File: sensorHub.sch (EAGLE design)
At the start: 11 parts

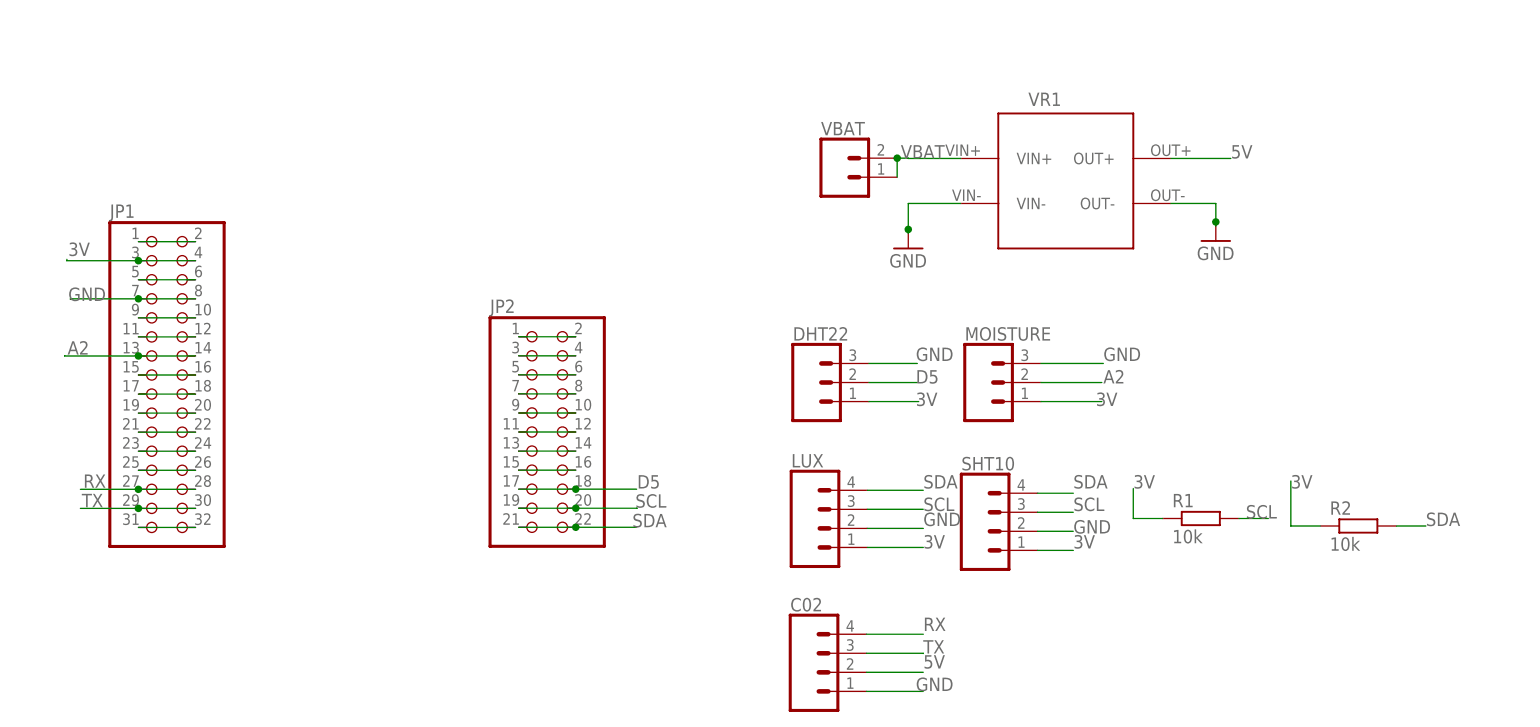
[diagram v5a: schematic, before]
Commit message: Connects the sht10 pins from SDA and SCL to pin 10 and pin 12 respectively
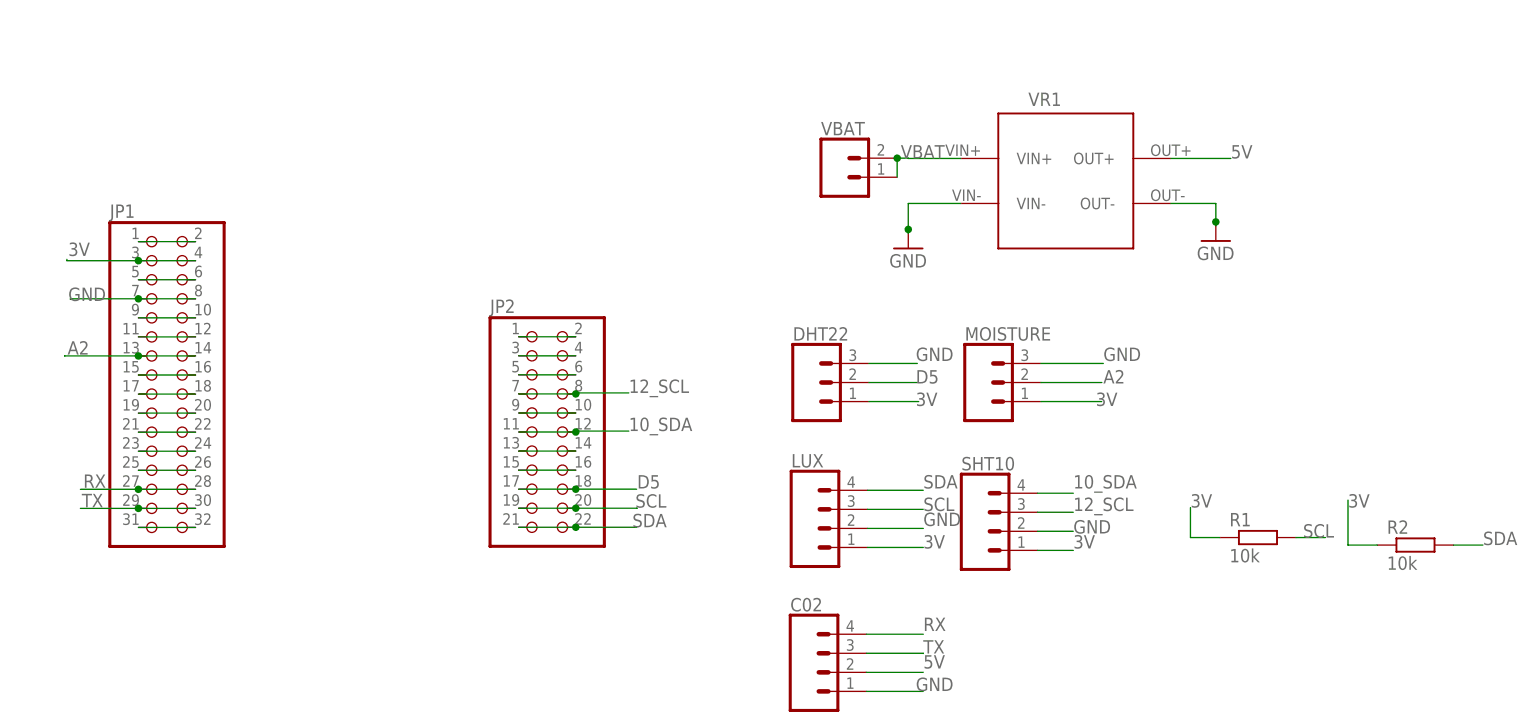
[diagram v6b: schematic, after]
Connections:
- removed net N$20: JP2.7, JP2.8
- removed net N$22: JP2.11, JP2.12
- new net 10_SDA: JP2.11, JP2.12, SHT10.4
- new net 12_SCL: JP2.7, JP2.8, SHT10.3
- net SCL: no longer SHT10.3
- net SDA: no longer SHT10.4
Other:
- moved on the sheet: R1, R2
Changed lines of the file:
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@@
 <attribute name="VALUE" x="132" y="95" size="1.778" layer="96"/>
 </instance>
-<instance part="R1" gate="G$1" x="155" y="62" smashed="yes">
-<attribute name="NAME" x="151.19" y="63.4986" size="1.778" layer="95"/>
-<attribute name="VALUE" x="151.19" y="58.698" size="1.778" layer="96"/>
-</instance>
-<instance part="R2" gate="G$1" x="176" y="61" smashed="yes">
-<attribute name="NAME" x="172.19" y="62.4986" size="1.778" layer="95"/>
-<attribute name="VALUE" x="172.19" y="57.698" size="1.778" layer="96"/>
+<instance part="R1" gate="G$1" x="162.62" y="59.46" smashed="yes">
+<attribute name="NAME" x="158.81" y="60.9586" size="1.778" layer="95"/>
+<attribute name="VALUE" x="158.81" y="56.158" size="1.778" layer="96"/>
+</instance>
+<instance part="R2" gate="G$1" x="183.62" y="58.46" smashed="yes">
+<attribute name="NAME" x="179.81" y="59.9586" size="1.778" layer="95"/>
+<attribute name="VALUE" x="179.81" y="55.158" size="1.778" layer="96"/>
 </instance>
 <instance part="DHT22" gate="J$1" x="103.14" y="80.13" smashed="yes">
@@
 <segment>
 <pinref part="R1" gate="G$1" pin="1"/>
-<wire x1="149.92" y1="62" x2="146" y2="62" width="0.1524" layer="91"/>
-<wire x1="146" y1="62" x2="146" y2="66" width="0.1524" layer="91"/>
-<label x="146" y="66" size="1.778" layer="95"/>
+<wire x1="157.54" y1="59.46" x2="153.62" y2="59.46" width="0.1524" layer="91"/>
+<wire x1="153.62" y1="59.46" x2="153.62" y2="63.46" width="0.1524" layer="91"/>
+<label x="153.62" y="63.46" size="1.778" layer="95"/>
 </segment>
 <segment>
 <pinref part="R2" gate="G$1" pin="1"/>
-<wire x1="170.92" y1="61" x2="167" y2="61" width="0.1524" layer="91"/>
-<wire x1="167" y1="61" x2="167" y2="67" width="0.1524" layer="91"/>
-<label x="167" y="66" size="1.778" layer="95"/>
+<wire x1="178.54" y1="58.46" x2="174.62" y2="58.46" width="0.1524" layer="91"/>
+<wire x1="174.62" y1="58.46" x2="174.62" y2="64.46" width="0.1524" layer="91"/>
+<label x="174.62" y="63.46" size="1.778" layer="95"/>
 </segment>
 </net>
@@
 </segment>
 </net>
-<net name="N$20" class="0">
-<segment>
-<pinref part="JP2" gate="A" pin="7"/>
-<pinref part="JP2" gate="A" pin="8"/>
-<wire x1="64.05" y1="78.61" x2="71.67" y2="78.61" width="0.1524" layer="91"/>
-</segment>
-</net>
 <net name="N$21" class="0">
 <segment>
@@
 <pinref part="JP2" gate="A" pin="10"/>
 <wire x1="64.05" y1="76.07" x2="71.67" y2="76.07" width="0.1524" layer="91"/>
-</segment>
-</net>
-<net name="N$22" class="0">
-<segment>
-<pinref part="JP2" gate="A" pin="11"/>
-<pinref part="JP2" gate="A" pin="12"/>
-<wire x1="64.05" y1="73.53" x2="71.67" y2="73.53" width="0.1524" layer="91"/>
 </segment>
 </net>
@@
 </segment>
 <segment>
-<pinref part="SHT10" gate="G$1" pin="3"/>
-<wire x1="133.23" y1="62.83" x2="138" y2="62.83" width="0.1524" layer="91"/>
-<label x="138" y="63" size="1.778" layer="95"/>
-</segment>
-<segment>
 <pinref part="R1" gate="G$1" pin="2"/>
-<wire x1="160.08" y1="62" x2="164" y2="62" width="0.1524" layer="91"/>
-<label x="161" y="62" size="1.778" layer="95"/>
+<wire x1="167.7" y1="59.46" x2="171.62" y2="59.46" width="0.1524" layer="91"/>
+<label x="168.62" y="59.46" size="1.778" layer="95"/>
 </segment>
 </net>
@@
 </segment>
 <segment>
-<pinref part="SHT10" gate="G$1" pin="4"/>
-<wire x1="133.23" y1="65.37" x2="138" y2="65.37" width="0.1524" layer="91"/>
-<label x="138" y="66" size="1.778" layer="95"/>
-</segment>
-<segment>
 <pinref part="R2" gate="G$1" pin="2"/>
-<wire x1="181.08" y1="61" x2="185" y2="61" width="0.1524" layer="91"/>
-<label x="185" y="61" size="1.778" layer="95"/>
+<wire x1="188.7" y1="58.46" x2="192.62" y2="58.46" width="0.1524" layer="91"/>
+<label x="192.62" y="58.46" size="1.778" layer="95"/>
 </segment>
 </net>
@@
 </segment>
 </net>
+<net name="10_SDA" class="0">
+<segment>
+<pinref part="SHT10" gate="G$1" pin="4"/>
+<wire x1="133.23" y1="65.37" x2="138" y2="65.37" width="0.1524" layer="91"/>
+<label x="138" y="66" size="1.778" layer="95"/>
+</segment>
+<segment>
+<pinref part="JP2" gate="A" pin="11"/>
+<pinref part="JP2" gate="A" pin="12"/>
+<wire x1="64.05" y1="73.53" x2="71.67" y2="73.53" width="0.1524" layer="91"/>
+<wire x1="71.67" y1="73.53" x2="71.67" y2="73.66" width="0.1524" layer="91"/>
+<wire x1="71.67" y1="73.66" x2="78.74" y2="73.66" width="0.1524" layer="91"/>
+<junction x="71.67" y="73.53"/>
+<label x="78.74" y="73.66" size="1.778" layer="95"/>
+</segment>
+</net>
+<net name="12_SCL" class="0">
+<segment>
+<pinref part="SHT10" gate="G$1" pin="3"/>
+<wire x1="133.23" y1="62.83" x2="138" y2="62.83" width="0.1524" layer="91"/>
+<label x="138" y="63" size="1.778" layer="95"/>
+</segment>
+<segment>
+<pinref part="JP2" gate="A" pin="7"/>
+<pinref part="JP2" gate="A" pin="8"/>
+<wire x1="64.05" y1="78.61" x2="71.67" y2="78.61" width="0.1524" layer="91"/>
+<wire x1="71.67" y1="78.61" x2="71.67" y2="78.74" width="0.1524" layer="91"/>
+<wire x1="71.67" y1="78.74" x2="78.74" y2="78.74" width="0.1524" layer="91"/>
+<junction x="71.67" y="78.61"/>
+<label x="78.74" y="78.74" size="1.778" layer="95"/>
+</segment>
+</net>

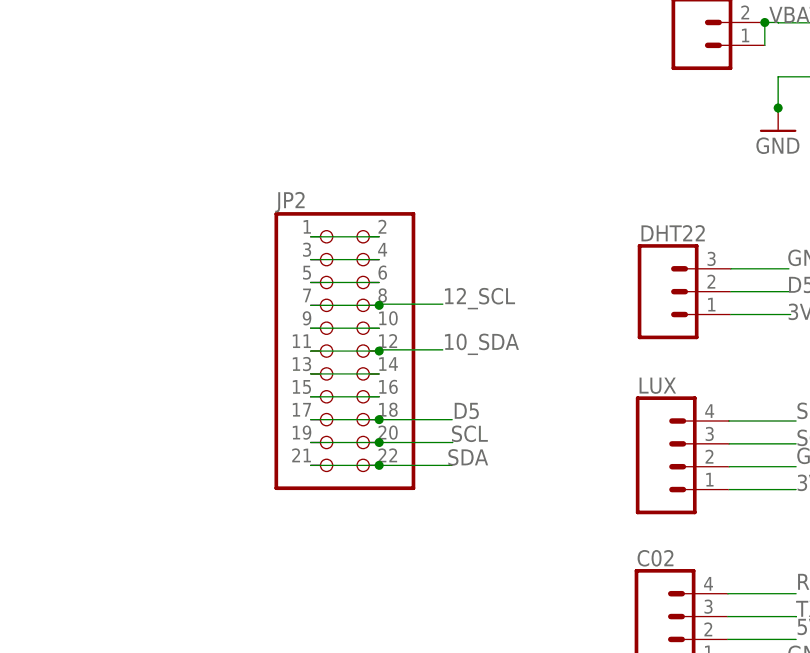
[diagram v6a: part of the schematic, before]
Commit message: Replaces the 22 double header with the 24 double header
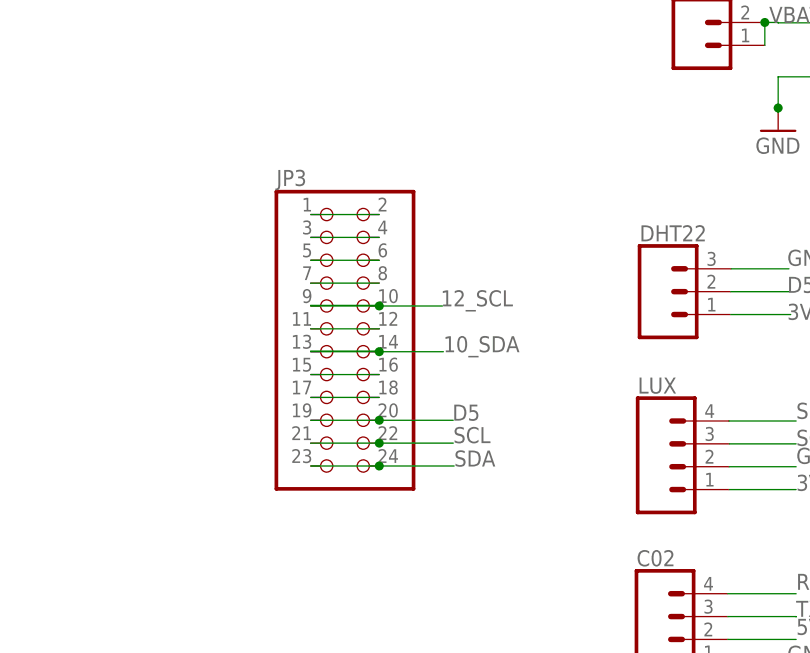
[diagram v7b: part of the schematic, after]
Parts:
- removed JP2: (no value), pinhead:PINHD-2X11
- added JP3: (no value), pinhead:PINHD-2X12
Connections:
- removed net N$19: JP2.5, JP2.6
- removed net N$21: JP2.10, JP2.9
- removed net N$23: JP2.13, JP2.14
- removed net N$24: JP2.15, JP2.16
- new net N$14: JP3.7, JP3.8
- new net N$15: JP3.11, JP3.12
- new net N$2: JP3.1, JP3.2
- new net N$4: JP3.3, JP3.4
- new net N$7: JP3.5, JP3.6
- net 10_SDA: now also JP3.13, JP3.14; no longer JP2.11, JP2.12
- net 12_SCL: now also JP3.10, JP3.9; no longer JP2.7, JP2.8
- net D5: now also JP3.19, JP3.20; no longer JP2.17, JP2.18
- net N$17: now also JP3.15, JP3.16; no longer JP2.1, JP2.2
- net N$18: now also JP3.17, JP3.18; no longer JP2.3, JP2.4
- net SCL: now also JP3.21, JP3.22; no longer JP2.19, JP2.20
- net SDA: now also JP3.23, JP3.24; no longer JP2.21, JP2.22
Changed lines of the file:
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@@
 <setting verticaltext="up"/>
 </settings>
-<grid distance="0.1" unitdist="inch" unit="inch" style="lines" multiple="1" display="no" altdistance="0.01" altunitdist="inch" altunit="inch"/>
+<grid distance="0.1" unitdist="mm" unit="mm" style="dots" multiple="1" display="yes" altdistance="1" altunitdist="mm" altunit="mm"/>
 <layers>
 <layer number="1" name="Top" color="4" fill="1" visible="no" active="no"/>
@@
 <parts>
 <part name="JP1" library="pinhead" library_urn="urn:adsk.eagle:library:325" deviceset="PINHD-2X16" device="" package3d_urn="urn:adsk.eagle:package:22431/2"/>
-<part name="JP2" library="pinhead" library_urn="urn:adsk.eagle:library:325" deviceset="PINHD-2X11" device="" package3d_urn="urn:adsk.eagle:package:22419/2"/>
 <part name="VR1" library="lm2577_module" deviceset="MT3608" device="THROUGH_HOLE"/>
 <part name="R1" library="resistor" library_urn="urn:adsk.eagle:library:348" deviceset="R-EU_" device="0207/10" package3d_urn="urn:adsk.eagle:package:25939/1" value="10k"/>
@@
 <part name="GND1" library="supply1" library_urn="urn:adsk.eagle:library:371" deviceset="GND" device=""/>
 <part name="GND2" library="supply1" library_urn="urn:adsk.eagle:library:371" deviceset="GND" device=""/>
+<part name="JP3" library="pinhead" library_urn="urn:adsk.eagle:library:325" deviceset="PINHD-2X12" device="" package3d_urn="urn:adsk.eagle:package:22420/2"/>
 </parts>
 <sheets>
@@
 <attribute name="VALUE" x="9.55" y="55.73" size="1.778" layer="96"/>
 </instance>
-<instance part="JP2" gate="A" x="66.59" y="73.53" smashed="yes">
-<attribute name="NAME" x="60.24" y="89.405" size="1.778" layer="95"/>
-<attribute name="VALUE" x="60.24" y="55.75" size="1.778" layer="96"/>
-</instance>
 <instance part="VR1" gate="G$1" x="137" y="107" smashed="yes">
 <attribute name="NAME" x="132" y="117" size="1.778" layer="95"/>
@@
 <instance part="GND2" gate="1" x="157" y="99" smashed="yes">
 <attribute name="VALUE" x="154.46" y="96.46" size="1.778" layer="96"/>
+</instance>
+<instance part="JP3" gate="A" x="66.6" y="76" smashed="yes">
+<attribute name="NAME" x="60.25" y="91.875" size="1.778" layer="95"/>
+<attribute name="VALUE" x="60.25" y="55.68" size="1.778" layer="96"/>
 </instance>
 </instances>
@@
 </segment>
 </net>
-<net name="N$17" class="0">
-<segment>
-<pinref part="JP2" gate="A" pin="1"/>
-<pinref part="JP2" gate="A" pin="2"/>
-<wire x1="64.05" y1="86.23" x2="71.67" y2="86.23" width="0.1524" layer="91"/>
-</segment>
-</net>
-<net name="N$18" class="0">
-<segment>
-<pinref part="JP2" gate="A" pin="3"/>
-<pinref part="JP2" gate="A" pin="4"/>
-<wire x1="64.05" y1="83.69" x2="71.67" y2="83.69" width="0.1524" layer="91"/>
-</segment>
-</net>
-<net name="N$19" class="0">
-<segment>
-<pinref part="JP2" gate="A" pin="5"/>
-<pinref part="JP2" gate="A" pin="6"/>
-<wire x1="64.05" y1="81.15" x2="71.67" y2="81.15" width="0.1524" layer="91"/>
-</segment>
-</net>
-<net name="N$21" class="0">
-<segment>
-<pinref part="JP2" gate="A" pin="9"/>
-<pinref part="JP2" gate="A" pin="10"/>
-<wire x1="64.05" y1="76.07" x2="71.67" y2="76.07" width="0.1524" layer="91"/>
-</segment>
-</net>
-<net name="N$23" class="0">
-<segment>
-<pinref part="JP2" gate="A" pin="13"/>
-<pinref part="JP2" gate="A" pin="14"/>
-<wire x1="64.05" y1="70.99" x2="71.67" y2="70.99" width="0.1524" layer="91"/>
-</segment>
-</net>
-<net name="N$24" class="0">
-<segment>
-<pinref part="JP2" gate="A" pin="15"/>
-<pinref part="JP2" gate="A" pin="16"/>
-<wire x1="64.05" y1="68.45" x2="71.67" y2="68.45" width="0.1524" layer="91"/>
-</segment>
-</net>
 <net name="D5" class="0">
-<segment>
-<pinref part="JP2" gate="A" pin="17"/>
-<pinref part="JP2" gate="A" pin="18"/>
-<wire x1="64.05" y1="65.91" x2="71.67" y2="65.91" width="0.1524" layer="91"/>
-<wire x1="71.67" y1="65.91" x2="79.79" y2="65.91" width="0.1524" layer="91"/>
-<junction x="71.67" y="65.91"/>
-<label x="79.85" y="66" size="1.778" layer="95"/>
-</segment>
 <segment>
 <pinref part="DHT22" gate="J$1" pin="2"/>
@@
 <label x="117" y="80" size="1.778" layer="95"/>
 </segment>
+<segment>
+<pinref part="JP3" gate="A" pin="19"/>
+<pinref part="JP3" gate="A" pin="20"/>
+<wire x1="64.06" y1="65.84" x2="71.68" y2="65.84" width="0.1524" layer="91"/>
+<wire x1="71.68" y1="65.84" x2="79.9" y2="65.84" width="0.1524" layer="91"/>
+<junction x="71.68" y="65.84"/>
+<label x="79.8" y="65.8" size="1.778" layer="95"/>
+</segment>
 </net>
 <net name="SCL" class="0">
-<segment>
-<pinref part="JP2" gate="A" pin="19"/>
-<pinref part="JP2" gate="A" pin="20"/>
-<wire x1="64.05" y1="63.37" x2="71.67" y2="63.37" width="0.1524" layer="91"/>
-<wire x1="71.67" y1="63.37" x2="79.83" y2="63.37" width="0.1524" layer="91"/>
-<wire x1="79.83" y1="63.37" x2="79.83" y2="63.39" width="0.1524" layer="91"/>
-<junction x="71.67" y="63.37"/>
-<label x="79.61" y="63.45" size="1.778" layer="95"/>
-</segment>
 <segment>
 <pinref part="LUX" gate="G$1" pin="3"/>
@@
 <label x="168.62" y="59.46" size="1.778" layer="95"/>
 </segment>
+<segment>
+<pinref part="JP3" gate="A" pin="21"/>
+<pinref part="JP3" gate="A" pin="22"/>
+<wire x1="64.06" y1="63.3" x2="71.68" y2="63.3" width="0.1524" layer="91"/>
+<wire x1="71.68" y1="63.3" x2="79.9" y2="63.3" width="0.1524" layer="91"/>
+<junction x="71.68" y="63.3"/>
+<label x="79.9" y="63.3" size="1.778" layer="95"/>
+</segment>
 </net>
 <net name="SDA" class="0">
-<segment>
-<pinref part="JP2" gate="A" pin="21"/>
-<pinref part="JP2" gate="A" pin="22"/>
-<wire x1="64.05" y1="60.83" x2="71.67" y2="60.83" width="0.1524" layer="91"/>
-<wire x1="71.67" y1="60.83" x2="79.79" y2="60.83" width="0.1524" layer="91"/>
-<junction x="71.67" y="60.83"/>
-<label x="79.21" y="60.83" size="1.778" layer="95"/>
-</segment>
 <segment>
 <pinref part="LUX" gate="G$1" pin="4"/>
@@
 <wire x1="188.7" y1="58.46" x2="192.62" y2="58.46" width="0.1524" layer="91"/>
 <label x="192.62" y="58.46" size="1.778" layer="95"/>
+</segment>
+<segment>
+<pinref part="JP3" gate="A" pin="23"/>
+<pinref part="JP3" gate="A" pin="24"/>
+<wire x1="64.06" y1="60.76" x2="71.68" y2="60.76" width="0.1524" layer="91"/>
+<wire x1="71.68" y1="60.76" x2="80" y2="60.76" width="0.1524" layer="91"/>
+<junction x="71.68" y="60.76"/>
+<label x="80" y="60.7" size="1.778" layer="95"/>
 </segment>
 </net>
@@
 </segment>
 <segment>
-<pinref part="JP2" gate="A" pin="11"/>
-<pinref part="JP2" gate="A" pin="12"/>
 <wire x1="64.05" y1="73.53" x2="71.67" y2="73.53" width="0.1524" layer="91"/>
 <wire x1="71.67" y1="73.53" x2="71.67" y2="73.66" width="0.1524" layer="91"/>
-<wire x1="71.67" y1="73.66" x2="78.74" y2="73.66" width="0.1524" layer="91"/>
-<junction x="71.67" y="73.53"/>
-<label x="78.74" y="73.66" size="1.778" layer="95"/>
+</segment>
+<segment>
+<pinref part="JP3" gate="A" pin="13"/>
+<pinref part="JP3" gate="A" pin="14"/>
+<wire x1="64.06" y1="73.46" x2="71.68" y2="73.46" width="0.1524" layer="91"/>
+<wire x1="71.68" y1="73.46" x2="78.8" y2="73.46" width="0.1524" layer="91"/>
+<junction x="71.68" y="73.46"/>
+<label x="78.8" y="73.4" size="1.778" layer="95"/>
 </segment>
 </net>
@@
 </segment>
 <segment>
-<pinref part="JP2" gate="A" pin="7"/>
-<pinref part="JP2" gate="A" pin="8"/>
 <wire x1="64.05" y1="78.61" x2="71.67" y2="78.61" width="0.1524" layer="91"/>
 <wire x1="71.67" y1="78.61" x2="71.67" y2="78.74" width="0.1524" layer="91"/>
-<wire x1="71.67" y1="78.74" x2="78.74" y2="78.74" width="0.1524" layer="91"/>
-<junction x="71.67" y="78.61"/>
-<label x="78.74" y="78.74" size="1.778" layer="95"/>
-</segment>
-</net>
+</segment>
+<segment>
+<pinref part="JP3" gate="A" pin="9"/>
+<pinref part="JP3" gate="A" pin="10"/>
+<wire x1="64.06" y1="78.54" x2="71.68" y2="78.54" width="0.1524" layer="91"/>
+<wire x1="71.68" y1="78.54" x2="78.7" y2="78.54" width="0.1524" layer="91"/>
+<junction x="71.68" y="78.54"/>
+<label x="78.5" y="78.5" size="1.778" layer="95"/>
+</segment>
+</net>
+<net name="N$2" class="0">
+<segment>
+<pinref part="JP3" gate="A" pin="1"/>
+<pinref part="JP3" gate="A" pin="2"/>
+<wire x1="64.06" y1="88.7" x2="71.68" y2="88.7" width="0.1524" layer="91"/>
+</segment>
+</net>
+<net name="N$4" class="0">
+<segment>
+<pinref part="JP3" gate="A" pin="3"/>
+<pinref part="JP3" gate="A" pin="4"/>
+<wire x1="64.06" y1="86.16" x2="71.68" y2="86.16" width="0.1524" layer="91"/>
+</segment>
+</net>
+<net name="N$7" class="0">
+<segment>
+<pinref part="JP3" gate="A" pin="5"/>
+<pinref part="JP3" gate="A" pin="6"/>
+<wire x1="64.06" y1="83.62" x2="71.68" y2="83.62" width="0.1524" layer="91"/>
+</segment>
+</net>
+<net name="N$14" class="0">
+<segment>
+<pinref part="JP3" gate="A" pin="7"/>
+<pinref part="JP3" gate="A" pin="8"/>
+<wire x1="64.06" y1="81.08" x2="71.68" y2="81.08" width="0.1524" layer="91"/>
+</segment>
+</net>
+<net name="N$15" class="0">
+<segment>
+<pinref part="JP3" gate="A" pin="11"/>
+<pinref part="JP3" gate="A" pin="12"/>
+<wire x1="64.06" y1="76" x2="71.68" y2="76" width="0.1524" layer="91"/>
+</segment>
+</net>
+<net name="N$17" class="0">
+<segment>
+<pinref part="JP3" gate="A" pin="15"/>
+<pinref part="JP3" gate="A" pin="16"/>
+<wire x1="64.06" y1="70.92" x2="71.68" y2="70.92" width="0.1524" layer="91"/>
+</segment>
+</net>
+<net name="N$18" class="0">
+<segment>
+<pinref part="JP3" gate="A" pin="17"/>
+<pinref part="JP3" gate="A" pin="18"/>
+<wire x1="64.06" y1="68.38" x2="71.68" y2="68.38" width="0.1524" layer="91"/>
+</segment>
+</net>
